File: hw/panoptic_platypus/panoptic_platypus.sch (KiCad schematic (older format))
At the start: 1 part, among them U1 MAX2851

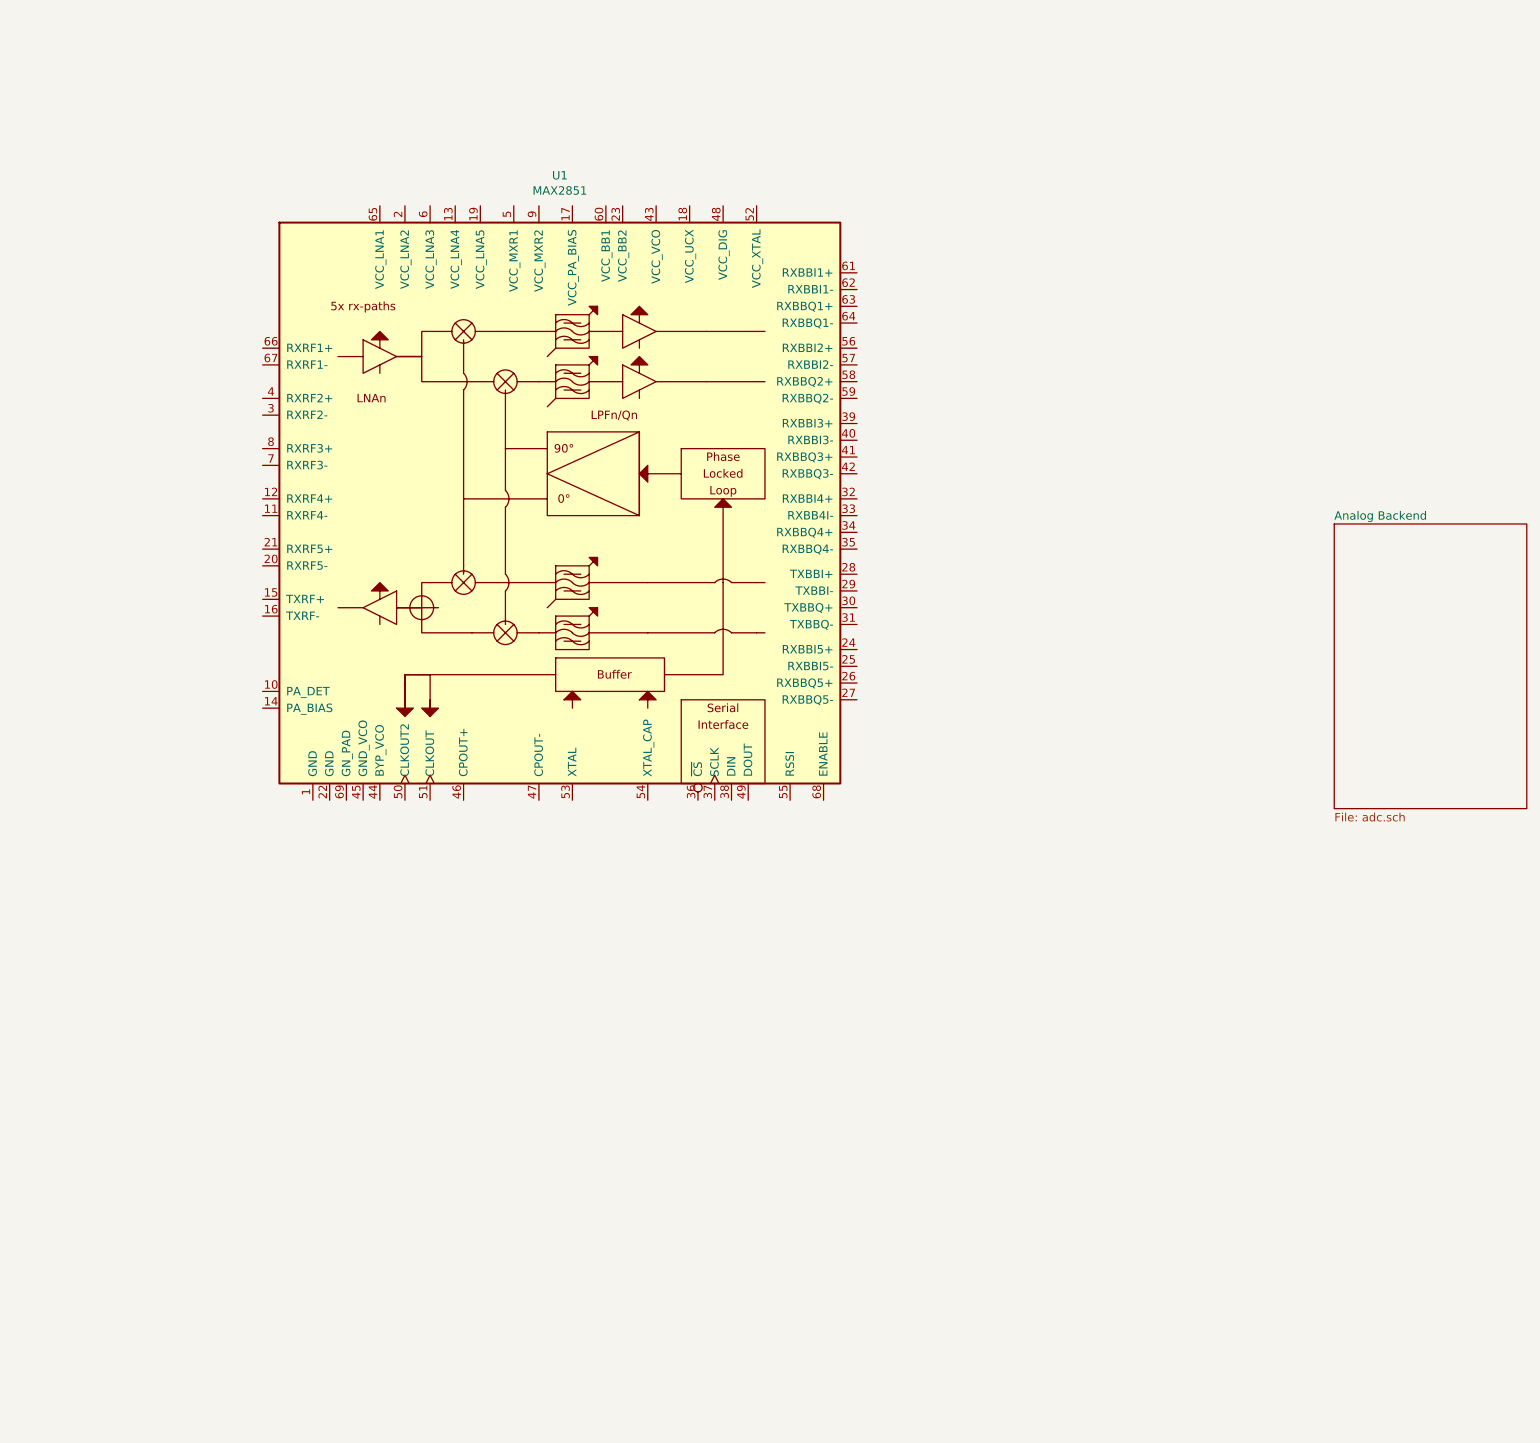
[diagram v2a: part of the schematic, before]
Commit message: updated some symbols added some ICs
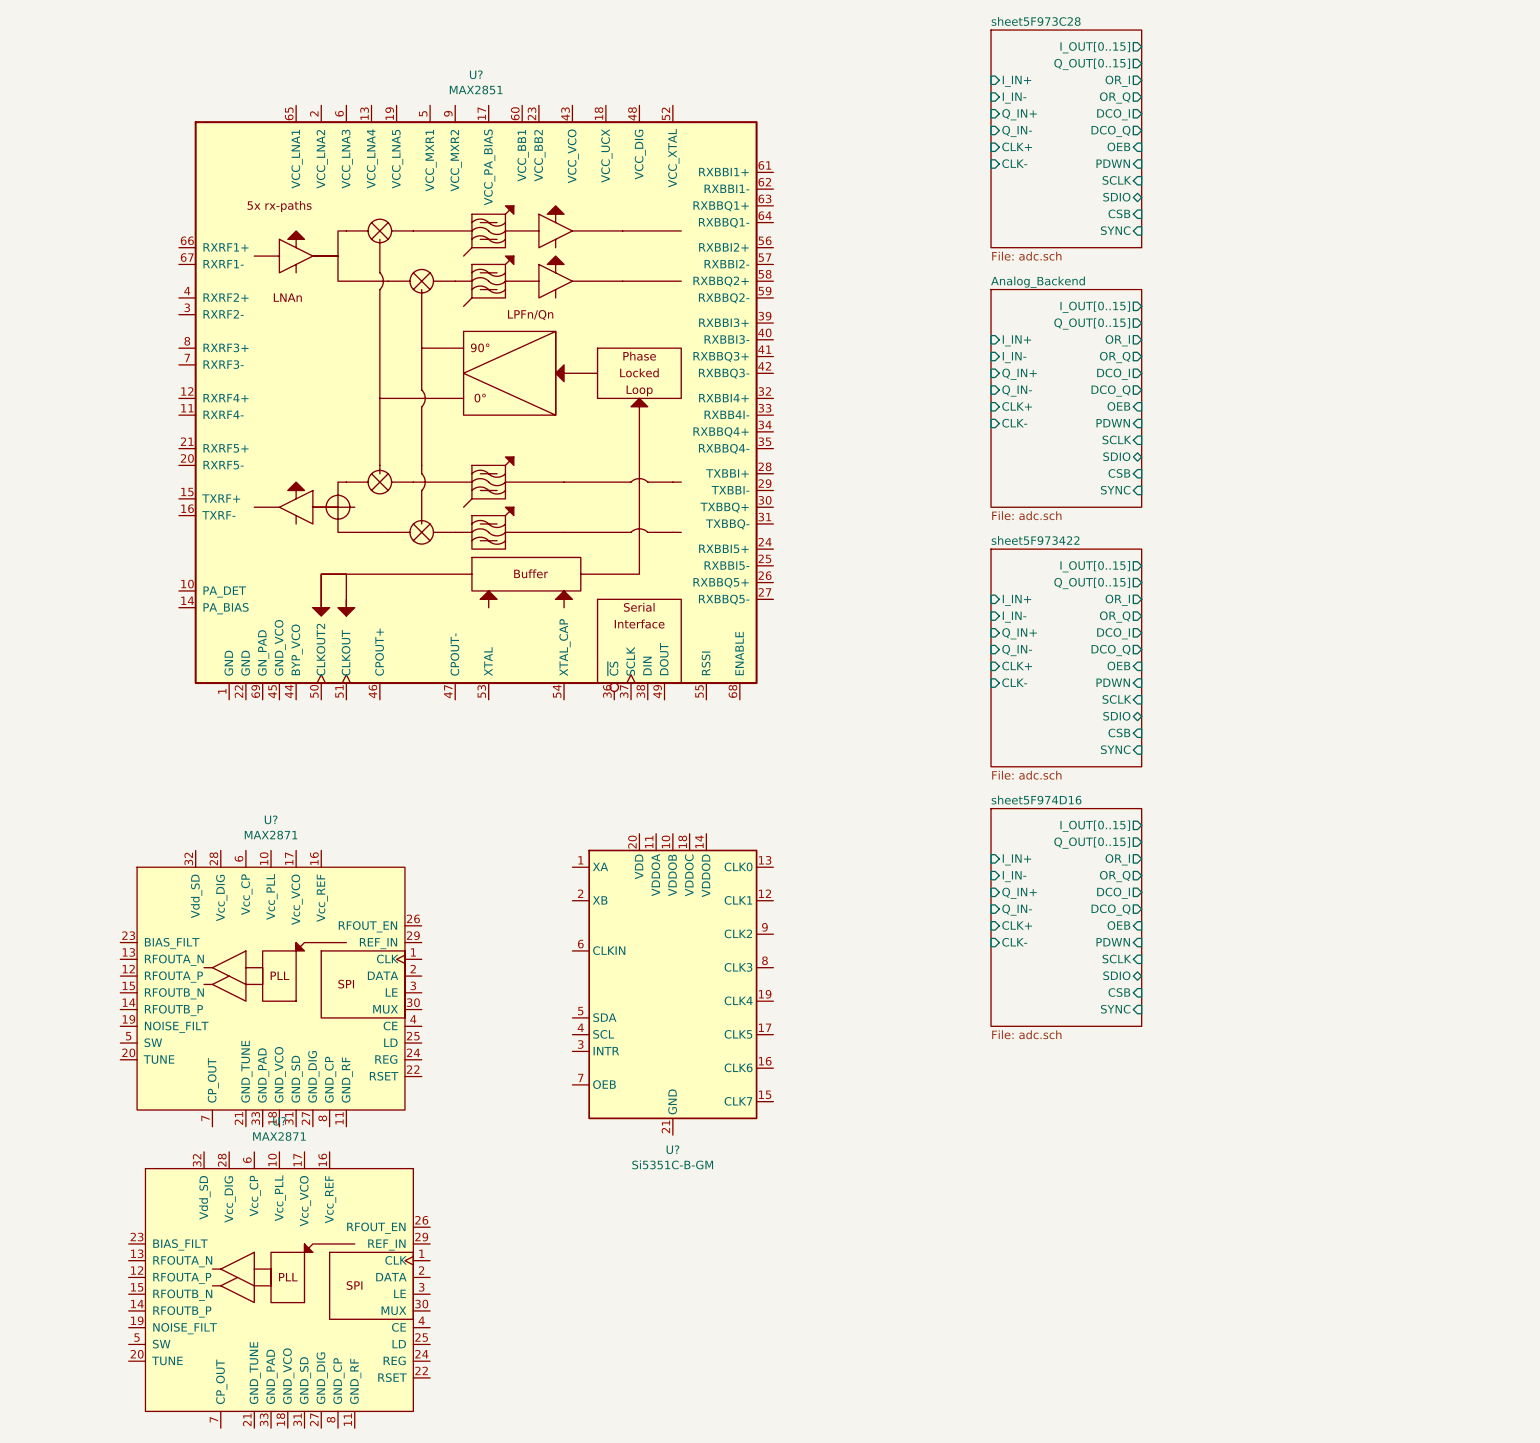
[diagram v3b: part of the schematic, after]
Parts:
- removed U1: MAX2851, symbol dknueppe_symbols:MAX2851
- added U?: MAX2851, symbol dknueppe_symbols:MAX2851
- added U? (x2): MAX2871, symbol dknueppe_symbols:MAX2871
- added U?: Si5351C-B-GM, Package_DFN_QFN:QFN-20-1EP_4x4mm_P0.5mm_EP2.7x2.7mm, symbol Oscillator:Si5351C-B-GM
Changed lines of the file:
@@
 $Descr A3 16535 11693
 encoding utf-8
-Sheet 1 6
+Sheet 1 9
 Title "Panoptic Platypus"
 Date "2020-09-21"
@@
 Comment4 ""
 $EndDescr
-$Comp
-L dknueppe_symbols:MAX2851 U1
-U 1 1 5F68B4A5
-P 5100 5500
-F 0 "U1" H 5075 7581 50  0000 C CNN
-F 1 "MAX2851" H 5075 7490 50  0000 C CNN
-F 2 "" H 3400 3800 50  0000 C CNN
-F 3 "" H 3400 3800 50  0001 C CNN
-	1    5100 5500
-	1    0    0    -1
-$EndComp
 $Sheet
 S 950  3150 500  800
@@
 $EndSheet
 $Sheet
-S 9700 5500 1150 1700
-U 5F6B2AD8
-F0 "Analog Backend" 50
-F1 "adc.sch" 50
-$EndSheet
+S 7650 4100 900  1300
+U 5F96EB25
+F0 "Analog_Backend" 50
+F1 "adc.sch" 50
+F2 "Q_OUT[0..15]" O R 8550 4300 50
+F3 "I_OUT[0..15]" O R 8550 4200 50
+F4 "CLK+" I L 7650 4800 50
+F5 "CLK-" I L 7650 4900 50
+F6 "SYNC" I R 8550 5300 50
+F7 "OR_I" O R 8550 4400 50
+F8 "DCO_I" O R 8550 4600 50
+F9 "I_IN+" I L 7650 4400 50
+F10 "I_IN-" I L 7650 4500 50
+F11 "Q_IN+" I L 7650 4600 50
+F12 "Q_IN-" I L 7650 4700 50
+F13 "OR_Q" O R 8550 4500 50
+F14 "DCO_Q" O R 8550 4700 50
+F15 "PDWN" I R 8550 4900 50
+F16 "SCLK" I R 8550 5000 50
+F17 "SDIO" B R 8550 5100 50
+F18 "OEB" I R 8550 4800 50
+F19 "CSB" I R 8550 5200 50
+$EndSheet
+$Sheet
+S 7650 5650 900  1300
+U 5F973436
+F0 "sheet5F973422" 50
+F1 "adc.sch" 50
+F2 "Q_OUT[0..15]" O R 8550 5850 50
+F3 "I_OUT[0..15]" O R 8550 5750 50
+F4 "CLK+" I L 7650 6350 50
+F5 "CLK-" I L 7650 6450 50
+F6 "SYNC" I R 8550 6850 50
+F7 "OR_I" O R 8550 5950 50
+F8 "DCO_I" O R 8550 6150 50
+F9 "I_IN+" I L 7650 5950 50
+F10 "I_IN-" I L 7650 6050 50
+F11 "Q_IN+" I L 7650 6150 50
+F12 "Q_IN-" I L 7650 6250 50
+F13 "OR_Q" O R 8550 6050 50
+F14 "DCO_Q" O R 8550 6250 50
+F15 "PDWN" I R 8550 6450 50
+F16 "SCLK" I R 8550 6550 50
+F17 "SDIO" B R 8550 6650 50
+F18 "OEB" I R 8550 6350 50
+F19 "CSB" I R 8550 6750 50
+$EndSheet
+$Sheet
+S 7650 2550 900  1300
+U 5F973C3C
+F0 "sheet5F973C28" 50
+F1 "adc.sch" 50
+F2 "Q_OUT[0..15]" O R 8550 2750 50
+F3 "I_OUT[0..15]" O R 8550 2650 50
+F4 "CLK+" I L 7650 3250 50
+F5 "CLK-" I L 7650 3350 50
+F6 "SYNC" I R 8550 3750 50
+F7 "OR_I" O R 8550 2850 50
+F8 "DCO_I" O R 8550 3050 50
+F9 "I_IN+" I L 7650 2850 50
+F10 "I_IN-" I L 7650 2950 50
+F11 "Q_IN+" I L 7650 3050 50
+F12 "Q_IN-" I L 7650 3150 50
+F13 "OR_Q" O R 8550 2950 50
+F14 "DCO_Q" O R 8550 3150 50
+F15 "PDWN" I R 8550 3350 50
+F16 "SCLK" I R 8550 3450 50
+F17 "SDIO" B R 8550 3550 50
+F18 "OEB" I R 8550 3250 50
+F19 "CSB" I R 8550 3650 50
+$EndSheet
+$Sheet
+S 7650 7200 900  1300
+U 5F974D2A
+F0 "sheet5F974D16" 50
+F1 "adc.sch" 50
+F2 "Q_OUT[0..15]" O R 8550 7400 50
+F3 "I_OUT[0..15]" O R 8550 7300 50
+F4 "CLK+" I L 7650 7900 50
+F5 "CLK-" I L 7650 8000 50
+F6 "SYNC" I R 8550 8400 50
+F7 "OR_I" O R 8550 7500 50
+F8 "DCO_I" O R 8550 7700 50
+F9 "I_IN+" I L 7650 7500 50
+F10 "I_IN-" I L 7650 7600 50
+F11 "Q_IN+" I L 7650 7700 50
+F12 "Q_IN-" I L 7650 7800 50
+F13 "OR_Q" O R 8550 7600 50
+F14 "DCO_Q" O R 8550 7800 50
+F15 "PDWN" I R 8550 8000 50
+F16 "SCLK" I R 8550 8100 50
+F17 "SDIO" B R 8550 8200 50
+F18 "OEB" I R 8550 7900 50
+F19 "CSB" I R 8550 8300 50
+$EndSheet
+$Comp
+L dknueppe_symbols:MAX2851 U?
+U 1 1 5F8D20C4
+P 4600 4900
+F 0 "U?" H 4575 6981 50  0000 C CNN
+F 1 "MAX2851" H 4575 6890 50  0000 C CNN
+F 2 "" H 3150 3850 50  0000 C CNN
+F 3 "" H 3150 3850 50  0001 C CNN
+	1    4600 4900
+	1    0    0    -1
+$EndComp
+$Comp
+L dknueppe_symbols:MAX2871 U?
+U 1 1 5F8F4A3C
+P 3350 8350
+F 0 "U?" H 3350 9431 50  0000 C CNN
+F 1 "MAX2871" H 3350 9340 50  0000 C CNN
+F 2 "" H 3350 9800 50  0001 C CNN
+F 3 "https://datasheets.maximintegrated.com/en/ds/MAX2871.pdf" H 3350 9800 50  0001 C CNN
+	1    3350 8350
+	1    0    0    -1
+$EndComp
+$Comp
+L Oscillator:Si5351C-B-GM U?
+U 1 1 5F90B22C
+P 5750 8250
+F 0 "U?" H 5750 7261 50  0000 C CNN
+F 1 "Si5351C-B-GM" H 5750 7170 50  0000 C CNN
+F 2 "Package_DFN_QFN:QFN-20-1EP_4x4mm_P0.5mm_EP2.7x2.7mm" H 5750 7050 50  0001 C CNN
+F 3 "https://www.silabs.com/documents/public/data-sheets/Si5351-B.pdf" H 5750 8250 50  0001 C CNN
+	1    5750 8250
+	1    0    0    -1
+$EndComp
+$Comp
+L dknueppe_symbols:MAX2871 U?
+U 1 1 5F90E31E
+P 3400 10150
+F 0 "U?" H 3400 11231 50  0000 C CNN
+F 1 "MAX2871" H 3400 11140 50  0000 C CNN
+F 2 "" H 3400 11600 50  0001 C CNN
+F 3 "https://datasheets.maximintegrated.com/en/ds/MAX2871.pdf" H 3400 11600 50  0001 C CNN
+	1    3400 10150
+	1    0    0    -1
+$EndComp
 $EndSCHEMATC

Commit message: Added LO Generator, fixed some smybols
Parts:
- removed U?: MAX2851, symbol dknueppe_symbols:MAX2851
- removed U? (x2): MAX2871, symbol dknueppe_symbols:MAX2871
- removed U?: Si5351C-B-GM, Package_DFN_QFN:QFN-20-1EP_4x4mm_P0.5mm_EP2.7x2.7mm, symbol Oscillator:Si5351C-B-GM
- added U1: MAX2851, dknueppe:TQFN-68_EP_10x10_Pitch0.5mm_EP7.7mmx7.7mm_ThermalVias, symbol dknueppe_symbols:MAX2851
- added U10: ECP5_5G_25_CABGA381, Package_BGA:Lattice_caBGA-381_17.0x17.0mm_Layout20x20_P0.8mm_Ball0.4mm_Pad0.4mm_NSMD, symbol dknueppe_symbols:ECP5_5G_25_CABGA381
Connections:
- new net GND: U1.1 (GND), U1.22 (GND), U1.44 (BYP_VCO), U1.45 (GND_VCO), U1.69 (GN_PAD)
- new net I_OUT0: U10.B20 (PT67B/-)
- new net I_OUT1: U10.B19 (PT65B/-)
- new net I_OUT10: U10.C16 (PT58A/+)
- new net I_OUT11: U10.A16 (PT56A/+)
- new net I_OUT12: U10.E15 (PT53B/-)
- new net I_OUT13: U10.C15 (PT51B/-)
- new net I_OUT14: U10.D15 (PT53A/+)
- new net I_OUT15: U10.B15 (PT51A/+)
- new net I_OUT2: U10.A19 (PT67A/+)
- new net I_OUT3: U10.A18 (PT65A/+)
- new net I_OUT4: U10.B18 (PT62B/-)
- new net I_OUT5: U10.C17 (PT60B/-)
- new net I_OUT6: U10.A17 (PT62A/+)
- new net I_OUT7: U10.B17 (PT60A/+)
- new net I_OUT8: U10.D16 (PT58B/-)
- new net I_OUT9: U10.B16 (PT56B/-)
- new net LO_Generator 1/REF_CLK_IN: U1.50 (CLKOUT2)
- new net LO_Generator 2/REF_CLK_IN: U1.51 (CLKOUT)
- new net Q_OUT0: U10.E14 (PT49B/-)
- new net Q_OUT1: U10.C14 (PT47B/-)
- new net Q_OUT10: U10.A12 (PT40A/+)
- new net Q_OUT11: U10.D12 (PT38A/+/GR_PCLK1_0)
- new net Q_OUT12: U10.C12 (PT35B/-/PCLKC1_0)
- new net Q_OUT13: U10.E11 (PT33B/-/PCLKC1_1)
- new net Q_OUT14: U10.B12 (PT35A/+/PCLKT1_0)
- new net Q_OUT15: U10.D11 (PT33A/+/PCLKT1_1)
- new net Q_OUT2: U10.D14 (PT49A/+)
- new net Q_OUT3: U10.A14 (PT47A/+)
- new net Q_OUT4: U10.E13 (PT44B/-)
- new net Q_OUT5: U10.C13 (PT42B/-)
- new net Q_OUT6: U10.D13 (PT44A/+)
- new net Q_OUT7: U10.B13 (PT42A/+)
- new net Q_OUT8: U10.A13 (PT40B/-)
- new net Q_OUT9: U10.E12 (PT38B/-/GR_PCLK1_1)

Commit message: added power supply, connected up some bits
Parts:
- added P?: USB_C_Plug, symbol Connector:USB_C_Plug
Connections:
- net ADC Path 1/I_IN+: now also U1.61 (RXBBI1+)
- net ADC Path 1/I_IN-: now also U1.62 (RXBBI1-)
- net ADC Path 1/Q_IN+: now also U1.63 (RXBBQ1+)
- net ADC Path 1/Q_IN-: now also U1.64 (RXBBQ1-)
- net ADC Path 3/I_IN+: now also U1.39 (RXBBI3+)
- net ADC Path 3/I_IN-: now also U1.40 (RXBBI3-)
- net ADC Path 3/Q_IN+: now also U1.41 (RXBBQ3+)
- net ADC Path 3/Q_IN-: now also U1.42 (RXBBQ3-)
- net ADC Path 4/I_IN+: now also U1.32 (RXBBI4+)
- net ADC Path 4/I_IN-: now also U1.33 (RXBB4I-)
- net ADC Path 4/Q_IN+: now also U1.34 (RXBBQ4+)
- net ADC Path 4/Q_IN-: now also U1.35 (RXBBQ4-)
- net ADC Path2/I_IN+: now also U1.56 (RXBBI2+)
- net ADC Path2/I_IN-: now also U1.57 (RXBBI2-)
- net ADC Path2/Q_IN+: now also U1.58 (RXBBQ2+)
- net ADC Path2/Q_IN-: now also U1.59 (RXBBQ2-)
- net GND: no longer U1.44 (BYP_VCO)
- net LO_Generator 1/REF_CLK_IN: no longer U1.50 (CLKOUT2)
- net LO_Generator 2/REF_CLK_IN: no longer U1.51 (CLKOUT)
- net Power/VCC_18_0: now reaches U10.F11 (VCCIO1)
- net Power/VCC_18_0: now also U10.F12 (VCCIO1), U10.H14 (VCCIO2), U10.H15 (VCCIO2), U10.J15 (VCCIO2), U10.L14 (VCCIO3), U10.L15 (VCCIO3), U10.L6 (VCCIO6), U10.L7 (VCCIO6), U10.M15 (VCCIO3), U10.M6 (VCCIO6)
- net Q_OUT_D15: now reaches U10.C18 (PR2A/+/HS/RDQ8)
- net I_OUT_D15: now reaches U10.C20 (PR14A/+/HS/RDQ20)
- net Q_OUT_D14: now reaches U10.D17 (PR2B/-/S0_IN/HS/RDQ8)
- net Q_OUT_D11: now reaches U10.D18 (PR5A/+/HS/RDQ8)
- net I_OUT_D13: now reaches U10.D19 (PR14B/-/HS/RDQ20)
- net I_OUT_D14: now reaches U10.D20 (PR14C/+/VREF1_2/RDQ20)
- net Q_OUT_D13: now reaches U10.E16 (PR2C/+/RDQ8)
- net Q_OUT_D9: now reaches U10.E17 (PR5B/-/HS/RDQ8)
- net Q_OUT_D10: now reaches U10.E18 (PR5C/+/RDQ8)
- net I_OUT_D12: now reaches U10.E19 (PR14D/-/RDQ20)
- net I_OUT_D11: now reaches U10.E20 (PR17A/+/HS/RDQ20)
- net Q_OUT_D12: now reaches U10.F16 (PR2D/-/RDQ8)
- net Q_OUT_D7: now reaches U10.F17 (PR8A/+/HS/RDQS8)
- net Q_OUT_D8: now reaches U10.F18 (PR5D/-/RDQ8)
- net I_OUT_D9: now reaches U10.F19 (PR17B/-/HS/RDQ20)
- net I_OUT_D10: now reaches U10.F20 (PR17C/+/RDQ20)
- net Q_OUT_D6: now reaches U10.G16 (PR8C/+/RDQ8)
- net Q_OUT_D5: now reaches U10.G18 (PR8B/-/HS/RDQSN8)
- net I_OUT_D7: now reaches U10.G19 (PR20A/+/GR_PCLK2_1/HS/RDQS20)
- net I_OUT_D8: now reaches U10.G20 (PR17D/-/RDQ20)
- net Q_OUT_D4: now reaches U10.H16 (PR8D/-/RDQ8)
- net Q_OUT_D1: now reaches U10.H17 (PR11B/-/HS/RDQ8)
- net Q_OUT_D3: now reaches U10.H18 (PR11A/+/HS/RDQ8)
- net I_OUT_D5: now reaches U10.H20 (PR20B/-/HS/RDQSN20)
- net Q_OUT_D0: now reaches U10.J16 (PR11D/-/RDQ8)
- net Q_OUT_D2: now reaches U10.J17 (PR11C/+/RDQ8)
- net I_OUT_D6: now reaches U10.J18 (PR20C/+/GR_PCLK2_0/RDQ20)
- net I_OUT_D3: now reaches U10.J19 (PR23A/+/PCLKT2_1/HS/RDQ20)
- net I_OUT_D2: now reaches U10.J20 (PR23C/+/PCLKT2_0/RDQ20)
- net I_OUT_D4: now reaches U10.K18 (PR20D/-/RDQ20)
- net I_OUT_D1: now reaches U10.K19 (PR23B/-/PCLKC2_1/HS/RDQ20)
- net I_OUT_D0: now reaches U10.K20 (PR23D/-/PCLKC2_0/RDQ20)
- net Q_OUT_B11: now reaches U10.L16 (PR29A/+/GR_PCLK3_0/HS/RDQ32)
- net Q_OUT_B9: now reaches U10.L17 (PR29B/-/HS/RDQ32)
- net Q_OUT_B10: now reaches U10.L18 (PR29C/+/GR_PCLK3_1/RDQ32)
- net Q_OUT_B14: now reaches U10.L19 (PR26C/+/PCLKT3_0/RDQ32)
- net Q_OUT_B15: now reaches U10.L20 (PR26A/+/PCLKT3_1/HS/RDQ32)
- net Q_OUT_B5: now reaches U10.M17 (PR32B/-/HS/RDQSN32)
- net Q_OUT_B8: now reaches U10.M18 (PR29D/-/RDQ32)
- net Q_OUT_B12: now reaches U10.M19 (PR26D/-/PCLKC3_0/RDQ32)
- net Q_OUT_B13: now reaches U10.M20 (PR26B/-/PCLKC3_1/HS/RDQ32)
- net Q_OUT_B7: now reaches U10.N16 (PR32A/+/HS/RDQS32)
- net Q_OUT_B3: now reaches U10.N17 (PR35A/+/HS/RDQ32)
- net Q_OUT_B6: now reaches U10.N18 (PR32C/+/RDQ32)
- net I_OUT_B15: now reaches U10.N19 (PR38A/+/HS/RDQ44)
- net I_OUT_B13: now reaches U10.N20 (PR38B/-/HS/RDQ44)
- net Q_OUT_B1: now reaches U10.P16 (PR35B/-/VREF1_3/HS/RDQ32)
- net Q_OUT_B4: now reaches U10.P17 (PR32D/-/RDQ32)
- net I_OUT_B12: now reaches U10.P18 (PR38D/-/RDQ44)
- net I_OUT_B14: now reaches U10.P19 (PR38C/+/RDQ44)
- net I_OUT_B11: now reaches U10.P20 (PR41A/+/HS/RDQ44)
- net Q_OUT_B2: now reaches U10.R16 (PR35C/+/RDQ32)
- net Q_OUT_B0: now reaches U10.R17 (PR35D/-/RDQ32)
- net I_OUT_B5: now reaches U10.R18 (PR44B/-/HS/RDQSN44)
- net I_OUT_B9: now reaches U10.R20 (PR41B/-/HS/RDQ44)
- net I_OUT_B0: now reaches U10.T17 (PR47D/-/LRC_GPLL0C_IN/RDQ44)
- net I_OUT_B4: now reaches U10.T18 (PR44D/-/RDQ44)
- net I_OUT_B7: now reaches U10.T19 (PR44A/+/HS/RDQS44)
- net I_OUT_B10: now reaches U10.T20 (PR41C/+/RDQ44)
- net I_OUT_B1: now reaches U10.U16 (PR47C/+/LRC_GPLL0T_IN/RDQ44)
- net I_OUT_B2: now reaches U10.U17 (PR47B/-/HS/RDQ44)
- net I_OUT_B3: now reaches U10.U18 (PR47A/+/HS/RDQ44)
- net I_OUT_B6: now reaches U10.U19 (PR44C/+/RDQ44)
- net I_OUT_B8: now reaches U10.U20 (PR41D/-/RDQ44)
- net I_OUT_C2: now reaches U10.F1 (PL26B/-/PCLKC6_1/HS/LDQ32)
- net I_OUT_C3: now reaches U10.G1 (PL26D/-/PCLKC6_0/LDQ32)
- net I_OUT_C0: now reaches U10.G2 (PL26A/+/PCLKT6_1/HS/LDQ32)
- net I_OUT_C9: now reaches U10.H1 (PL32C/+/LDQ32)
- net I_OUT_C1: now reaches U10.H2 (PL26C/+/PCLKT6_0/LDQ32)
- net I_OUT_C10: now reaches U10.J1 (PL32B/-/HS/LDQSN32)
- net I_OUT_C5: now reaches U10.J3 (PL29C/+/GR_PCLK6_1/LDQ32)
- net I_OUT_C4: now reaches U10.J4 (PL29A/+/GR_PCLK6_0/HS/LDQ32)
- net I_OUT_C6: now reaches U10.J5 (PL29B/-/HS/LDQ32)
- net I_OUT_C11: now reaches U10.K1 (PL32D/-/LDQ32)
- net I_OUT_C8: now reaches U10.K2 (PL32A/+/HS/LDQS32)
- net I_OUT_C7: now reaches U10.K3 (PL29D/-/LDQ32)
- net I_OUT_C12: now reaches U10.K4 (PL35A/+/HS/LDQ32)
- net I_OUT_C14: now reaches U10.K5 (PL35B/-/VREF1_6/HS/LDQ32)
- net Q_OUT_C9: now reaches U10.L1 (PL44C/+/LDQ44)
- net Q_OUT_C7: now reaches U10.L2 (PL41D/-/LDQ44)
- net Q_OUT_C5: now reaches U10.L3 (PL41C/+/LDQ44)
- net I_OUT_C13: now reaches U10.L4 (PL35C/+/LDQ32)
- net I_OUT_C15: now reaches U10.L5 (PL35D/-/LDQ32)
- net Q_OUT_C10: now reaches U10.M1 (PL44B/-/HS/LDQSN44)
- net Q_OUT_C6: now reaches U10.M3 (PL41B/-/HS/LDQ44)
- net Q_OUT_C0: now reaches U10.M4 (PL38A/+/HS/LDQ44)
- net Q_OUT_C11: now reaches U10.N1 (PL44D/-/LDQ44)
- net Q_OUT_C8: now reaches U10.N2 (PL44A/+/HS/LDQS44)
- net Q_OUT_C4: now reaches U10.N3 (PL41A/+/HS/LDQ44)
- net Q_OUT_C1: now reaches U10.N4 (PL38C/+/LDQ44)
- net Q_OUT_C2: now reaches U10.N5 (PL38B/-/HS/LDQ44)
- net Q_OUT_C12: now reaches U10.P1 (PL47A/+/HS/LDQ44)
- net Q_OUT_C13: now reaches U10.P2 (PL47B/-/HS/LDQ44)
- net Q_OUT_C14: now reaches U10.P3 (PL47C/+/LLC_GPLL0T_IN/LDQ44)
- net Q_OUT_C15: now reaches U10.P4 (PL47D/-/LLC_GPLL0C_IN/LDQ44)
- net Q_OUT_C3: now reaches U10.P5 (PL38D/-/LDQ44)
- net I_OUT0 renamed I_OUT_A0
- net I_OUT1 renamed I_OUT_A1
- net I_OUT10 renamed I_OUT_A10
- net I_OUT11 renamed I_OUT_A11
- net I_OUT12 renamed I_OUT_A12
- net I_OUT13 renamed I_OUT_A13
- net I_OUT14 renamed I_OUT_A14
- net I_OUT15 renamed I_OUT_A15
- net I_OUT2 renamed I_OUT_A2
- net I_OUT3 renamed I_OUT_A3
- net I_OUT4 renamed I_OUT_A4
- net I_OUT5 renamed I_OUT_A5
- net I_OUT6 renamed I_OUT_A6
- net I_OUT7 renamed I_OUT_A7
- net I_OUT8 renamed I_OUT_A8
- net I_OUT9 renamed I_OUT_A9
- net Q_OUT0 renamed O_OUT_A0
- net Q_OUT1 renamed O_OUT_A1
- net Q_OUT10 renamed O_OUT_A10
- net Q_OUT11 renamed O_OUT_A11
- net Q_OUT12 renamed O_OUT_A12
- net Q_OUT13 renamed O_OUT_A13
- net Q_OUT14 renamed O_OUT_A14
- net Q_OUT15 renamed O_OUT_A15
- net Q_OUT2 renamed O_OUT_A2
- net Q_OUT3 renamed O_OUT_A3
- net Q_OUT4 renamed O_OUT_A4
- net Q_OUT5 renamed O_OUT_A5
- net Q_OUT6 renamed O_OUT_A6
- net Q_OUT7 renamed O_OUT_A7
- net Q_OUT8 renamed O_OUT_A8
- net Q_OUT9 renamed O_OUT_A9
- new net: P?.A1 (GND), P?.A12 (GND), P?.B1 (GND), P?.B12 (GND)
- new net: P?.A4 (VBUS), P?.A9 (VBUS), P?.B4 (VBUS), P?.B9 (VBUS)
- no-connect marks 0 -> 12
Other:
- moved on the sheet: U10B, U10H, U10I, U10J
